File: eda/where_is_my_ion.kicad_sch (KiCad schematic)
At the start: 130 parts, among them J1 USB_C_Receptacle_USB2.0_14P, Q1 Q_NPN, Q2 Q_NPN, SW1 SW_SPST, SW2 SW_SPST, U1 ESP32-C3-WROOM-02, U2 AP2112K-3.3, U3 CP2102N-Axx-xQFN28, U4 TLC59116IPWR, U5 TLC59116IPWR, U6 TLC59116IPWR, U7 TLC59116IPWR, U8 TLC59116IPWR

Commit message: final sch
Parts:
- added C14, C16, C18, C20, C22: 0.1uF ceramic, symbol Device:C
- added C15, C17, C19, C21, C23: 10uF, symbol Device:C
- added D69, D84, D85: LED, symbol Device:LED
- added SW3: FORCE_REFRESH, symbol Switch:SW_Push
- added SW4: NEXT_TRAIN, symbol Switch:SW_Push
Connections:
- net +3V3: now also D68.2 (A), D70.2 (A), D72.2 (A), D73.2 (A), D74.2 (A), D75.2 (A), D76.2 (A), D77.2 (A), D78.2 (A), D79.2 (A), D80.2 (A), D81.2 (A), D82.2 (A), D83.2 (A), U5.2 (A0), U6.3 (A1), U7.2 (A0), U7.3 (A1), U8.4 (A2), C14.1, C15.1, C16.1, C17.1, C18.1, C19.1, C20.1, C21.1, C22.1, C23.1, D69.2 (A), D84.2 (A), D85.2 (A)
- net CHIP_PU: now also C11.2, SW2.2 (B)
- net GND: now also U6.2 (A0), U6.4 (A2), U6.5 (A3), C14.2, C15.2, C16.2, C17.2, C18.2, C19.2, C20.2, C21.2, C22.2, C23.2, SW3.2, SW4.2; no longer U5.2 (A0), U7.2 (A0), U7.3 (A1), U8.4 (A2)
- net IO11: now also SW3.1
- net IO12: now also SW4.1
- net LED_IS_FETCHING: now reaches U5.22 (~{OUT14})
- net LED_IS_FETCHING: now also D69.1 (K)
- net LED_MAP_MODE: now reaches U8.22 (~{OUT14})
- net LED_MAP_MODE: now also D84.1 (K)
- net LED_API_FAILURE: now reaches U8.23 (~{OUT15})
- net LED_API_FAILURE: now also D85.1 (K)
- no-connect marks 21 -> 18
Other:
- note added: "CORE ESP MCU"
- note added: "I2C PULL UP RESISTORS"
- note added: "LED DRIVER 1"
- note added: "LED DRIVER 2"
- note added: "LED DRIVER 3"
- note added: "LED DRIVER 4"
- note added: "LED DRIVER 5"
- note removed: "CORE MODULE"
- moved on the sheet: C1, C10, C11, C2, C3, C4, C5, C6, C7, C8, C9, D1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

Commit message: stuff
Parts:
- removed J1: USB_C_Receptacle_USB2.0_14P, symbol Connector:USB_C_Receptacle_USB2.0_14P
- removed Q1, Q2: Q_NPN, symbol Device:Q_NPN
- added H1, H2, H3, H4: MountingHole, MountingHole:MountingHole_2.2mm_M2, symbol Mechanical:MountingHole
- added J1: USB_C_Receptacle_USB2.0_16P, Connector_USB:USB_C_Receptacle_HRO_TYPE-C-31-M-12, symbol Connector:USB_C_Receptacle_USB2.0_16P
- added Q1, Q2: L8050QLT1G, Package_TO_SOT_SMD:SOT-23, symbol Transistor_BJT:Q_NPN_BEC
- added TP1, TP2, TP3, TP4, TP5, TP6, TP7, TP8, TP9: TestPoint, TestPoint:TestPoint_Pad_D2.0mm, symbol Connector:TestPoint
- C1: renamed from C8; footprint (none) -> Capacitor_Tantalum_SMD:CP_EIA-3528-15_AVX-H; LCSC Part Num. (none) -> C22387953
- C10: renamed from C21; footprint (none) -> Capacitor_Tantalum_SMD:CP_EIA-3528-15_AVX-H
- C11: renamed from C10; footprint (none) -> Capacitor_SMD:C_0805_2012Metric; LCSC Part Num. (none) -> C376929
- C12: renamed from C1; value 10uF -> 10uF/25V; footprint (none) -> Capacitor_Tantalum_SMD:CP_EIA-3528-15_AVX-H; LCSC Part Num. (none) -> C22387953
- C13: renamed from C2; value C -> 0.1uF/50V; footprint (none) -> Capacitor_SMD:C_0603_1608Metric; LCSC Part Num. (none) -> C3011652
- C14: renamed from C3; value C -> 1uF/16V; footprint (none) -> Capacitor_SMD:C_0805_2012Metric; LCSC Part Num. (none) -> C24123
- C15: renamed from C11; footprint (none) -> Capacitor_SMD:C_0805_2012Metric; LCSC Part Num. (none) -> C376929
- C16: renamed from C22; footprint (none) -> Capacitor_SMD:C_0603_1608Metric
- C17: renamed from C23; footprint (none) -> Capacitor_Tantalum_SMD:CP_EIA-3528-15_AVX-H
- C18: renamed from C7; value 10 uFF/25V -> 10 uF/25V; footprint (none) -> Capacitor_Tantalum_SMD:CP_EIA-3528-15_AVX-H
- C19: renamed from C6; footprint (none) -> Capacitor_SMD:C_0603_1608Metric
- C2: renamed from C14; footprint (none) -> Capacitor_SMD:C_0603_1608Metric
- C20: renamed from C4; footprint (none) -> Capacitor_SMD:C_0603_1608Metric
- C21: renamed from C5; footprint (none) -> Capacitor_Tantalum_SMD:CP_EIA-3528-15_AVX-H
- C3: renamed from C15; footprint (none) -> Capacitor_Tantalum_SMD:CP_EIA-3528-15_AVX-H
- C4: renamed from C18; footprint (none) -> Capacitor_SMD:C_0603_1608Metric
- C5: renamed from C19; footprint (none) -> Capacitor_Tantalum_SMD:CP_EIA-3528-15_AVX-H
- C6: renamed from C9; footprint (none) -> Capacitor_SMD:C_0805_2012Metric; LCSC Part Num. (none) -> C24123
- C7: renamed from C16; footprint (none) -> Capacitor_SMD:C_0603_1608Metric
- C8: renamed from C17; footprint (none) -> Capacitor_Tantalum_SMD:CP_EIA-3528-15_AVX-H
- C9: renamed from C20; footprint (none) -> Capacitor_SMD:C_0603_1608Metric
- D1: renamed from D17; value LED -> LED_STN_BLUE; footprint (none) -> LED_SMD:LED_0603_1608Metric; LCSC Part Num. (none) -> C497940
- D10: renamed from D38; value LED -> LED_INTER_WHITE; footprint (none) -> LED_SMD:LED_0603_1608Metric
- D11: renamed from D40; value LED -> LED_INTER_WHITE; footprint (none) -> LED_SMD:LED_0603_1608Metric
- D12: renamed from D42; value LED -> LED_INTER_WHITE; footprint (none) -> LED_SMD:LED_0603_1608Metric
- D13: renamed from D44; value LED -> LED_STN_BLUE; footprint (none) -> LED_SMD:LED_0603_1608Metric
- D14: renamed from D46; value LED -> LED_INTER_WHITE; footprint (none) -> LED_SMD:LED_0603_1608Metric
- D15: renamed from D48; value LED -> LED_INTER_WHITE; footprint (none) -> LED_SMD:LED_0603_1608Metric
- D16: renamed from D50; value LED -> LED_INTER_WHITE; footprint (none) -> LED_SMD:LED_0603_1608Metric
- D17: renamed from D18; value LED -> LED_STN_BLUE; footprint (none) -> LED_SMD:LED_0603_1608Metric
- D18: renamed from D19; value LED -> LED_STN_BLUE; footprint (none) -> LED_SMD:LED_0603_1608Metric
- D19: renamed from D20; value LED -> LED_INTER_WHITE; footprint (none) -> LED_SMD:LED_0603_1608Metric
- D2: renamed from D16; value LED -> LED_INTER_WHITE; footprint (none) -> LED_SMD:LED_0603_1608Metric; LCSC Part Num. (none) -> C965808
- D20: renamed from D21; value LED -> LED_STN_BLUE; footprint (none) -> LED_SMD:LED_0603_1608Metric
- D21: renamed from D10; value LED -> LED_INTER_WHITE; footprint (none) -> LED_SMD:LED_0603_1608Metric
- D22: renamed from D11; value LED -> LED_STN_BLUE; footprint (none) -> LED_SMD:LED_0603_1608Metric
- D23: renamed from D12; value LED -> LED_INTER_WHITE; footprint (none) -> LED_SMD:LED_0603_1608Metric
- D24: renamed from D13; value LED -> LED_INTER_WHITE; footprint (none) -> LED_SMD:LED_0603_1608Metric
- D25, D59, D7, D77: value LED -> LED_INTER_WHITE; footprint (none) -> LED_SMD:LED_0603_1608Metric
- D26: renamed from D39; value LED -> LED_INTER_WHITE; footprint (none) -> LED_SMD:LED_0603_1608Metric
- D27: renamed from D41; value LED -> LED_INTER_WHITE; footprint (none) -> LED_SMD:LED_0603_1608Metric
- D28: renamed from D43; value LED -> LED_STN_BLUE; footprint (none) -> LED_SMD:LED_0603_1608Metric
- D29: renamed from D45; value LED -> LED_INTER_WHITE; footprint (none) -> LED_SMD:LED_0603_1608Metric
- D3: renamed from D15; value LED -> LED_INTER_WHITE; footprint (none) -> LED_SMD:LED_0603_1608Metric
- D30: renamed from D47; value LED -> LED_INTER_WHITE; footprint (none) -> LED_SMD:LED_0603_1608Metric
- D31: renamed from D49; value LED -> LED_INTER_WHITE; footprint (none) -> LED_SMD:LED_0603_1608Metric
- D32: renamed from D51; value LED -> LED_STN_BLUE; footprint (none) -> LED_SMD:LED_0603_1608Metric
- D33: renamed from D22; value LED -> LED_STN_BLUE; footprint (none) -> LED_SMD:LED_0603_1608Metric
- D34: renamed from D24; value LED -> LED_STN_BLUE; footprint (none) -> LED_SMD:LED_0603_1608Metric
- D35: renamed from D26; value LED -> LED_STN_BLUE; footprint (none) -> LED_SMD:LED_0603_1608Metric
- D36: renamed from D28; value LED -> LED_STN_BLUE; footprint (none) -> LED_SMD:LED_0603_1608Metric
- D37: renamed from D30; value LED -> LED_INTER_WHITE; footprint (none) -> LED_SMD:LED_0603_1608Metric
- D38: renamed from D32; value LED -> LED_INTER_WHITE; footprint (none) -> LED_SMD:LED_0603_1608Metric
- D39: renamed from D34; value LED -> LED_STN_BLUE; footprint (none) -> LED_SMD:LED_0603_1608Metric
- D4: renamed from D14; value LED -> LED_INTER_WHITE; footprint (none) -> LED_SMD:LED_0603_1608Metric
- D40: renamed from D36; value LED -> LED_INTER_WHITE; footprint (none) -> LED_SMD:LED_0603_1608Metric
- D41: renamed from D52; value LED -> LED_STN_BLUE; footprint (none) -> LED_SMD:LED_0603_1608Metric
- D42: renamed from D54; value LED -> LED_STN_BLUE; footprint (none) -> LED_SMD:LED_0603_1608Metric
- D43: renamed from D56; value LED -> LED_STN_BLUE; footprint (none) -> LED_SMD:LED_0603_1608Metric
- D44: renamed from D58; value LED -> LED_INTER_WHITE; footprint (none) -> LED_SMD:LED_0603_1608Metric
- D45: renamed from D60; value LED -> LED_INTER_WHITE; footprint (none) -> LED_SMD:LED_0603_1608Metric
- D46: renamed from D62; value LED -> LED_STN_BLUE; footprint (none) -> LED_SMD:LED_0603_1608Metric
- D47: renamed from D64; value LED -> LED_INTER_WHITE; footprint (none) -> LED_SMD:LED_0603_1608Metric
- D48: renamed from D66; value LED -> LED_STN_BLUE; footprint (none) -> LED_SMD:LED_0603_1608Metric
- D49: renamed from D69; value LED -> LED_FETCH_GREEN; footprint (none) -> LED_SMD:LED_0603_1608Metric; LCSC Part Num. (none) -> C7429914
- D5: renamed from D9; value LED -> LED_STN_BLUE; footprint (none) -> LED_SMD:LED_0603_1608Metric
- D50: renamed from D27; value LED -> LED_STN_BLUE; footprint (none) -> LED_SMD:LED_0603_1608Metric
- D51: renamed from D29; value LED -> LED_INTER_WHITE; footprint (none) -> LED_SMD:LED_0603_1608Metric
- D52: renamed from D31; value LED -> LED_INTER_WHITE; footprint (none) -> LED_SMD:LED_0603_1608Metric
- D53: renamed from D33; value LED -> LED_STN_BLUE; footprint (none) -> LED_SMD:LED_0603_1608Metric
- D54: renamed from D35; value LED -> LED_INTER_WHITE; footprint (none) -> LED_SMD:LED_0603_1608Metric
- D55: renamed from D37; value LED -> LED_INTER_WHITE; footprint (none) -> LED_SMD:LED_0603_1608Metric
- D56: renamed from D53; value LED -> LED_INTER_WHITE; footprint (none) -> LED_SMD:LED_0603_1608Metric
- D57: renamed from D55; value LED -> LED_STN_BLUE; footprint (none) -> LED_SMD:LED_0603_1608Metric
- D58: renamed from D57; value LED -> LED_STN_BLUE; footprint (none) -> LED_SMD:LED_0603_1608Metric
- D6: renamed from D8; value LED -> LED_INTER_WHITE; footprint (none) -> LED_SMD:LED_0603_1608Metric
- D60: renamed from D61; value LED -> LED_STN_BLUE; footprint (none) -> LED_SMD:LED_0603_1608Metric
- D61: renamed from D63; value LED -> LED_INTER_WHITE; footprint (none) -> LED_SMD:LED_0603_1608Metric
- D62: renamed from D65; value LED -> LED_INTER_WHITE; footprint (none) -> LED_SMD:LED_0603_1608Metric
- D63: renamed from D67; value LED -> LED_STN_BLUE; footprint (none) -> LED_SMD:LED_0603_1608Metric
- D64: renamed from D68; value LED -> LED_INTER_WHITE; footprint (none) -> LED_SMD:LED_0603_1608Metric
- D65: renamed from D70; value LED -> LED_INTER_WHITE; footprint (none) -> LED_SMD:LED_0603_1608Metric
- D66: renamed from D72; value LED -> LED_STN_BLUE; footprint (none) -> LED_SMD:LED_0603_1608Metric
- D67: renamed from D74; value LED -> LED_INTER_WHITE; footprint (none) -> LED_SMD:LED_0603_1608Metric
- D68: renamed from D76; value LED -> LED_INTER_WHITE; footprint (none) -> LED_SMD:LED_0603_1608Metric
- D69: renamed from D78; value LED -> LED_INTER_WHITE; footprint (none) -> LED_SMD:LED_0603_1608Metric
- D70: renamed from D80; value LED -> LED_INTER_WHITE; footprint (none) -> LED_SMD:LED_0603_1608Metric
- D71: renamed from D82; value LED -> LED_STN_BLUE; footprint (none) -> LED_SMD:LED_0603_1608Metric
- D72: renamed from D2; footprint (none) -> Diode_SMD:D_SOD-123; LCSC Part Num. (none) -> C82544
- D73: renamed from D85; value LED -> LED_API_FAIL_RED; footprint (none) -> LED_SMD:LED_0603_1608Metric
- D74: renamed from D84; value LED -> LED_MAP_MODE_GREEN; footprint (none) -> LED_SMD:LED_0603_1608Metric
- D75: renamed from D73; value LED -> LED_GREEN_WIFI; footprint (none) -> LED_SMD:LED_0603_1608Metric
- D76: renamed from D75; value LED -> LED_STN_BLUE; footprint (none) -> LED_SMD:LED_0603_1608Metric
- D78: renamed from D79; value LED -> LED_INTER_WHITE; footprint (none) -> LED_SMD:LED_0603_1608Metric
- D79: renamed from D81; value LED -> LED_INTER_WHITE; footprint (none) -> LED_SMD:LED_0603_1608Metric
- D8: renamed from D6; value LED -> LED_STN_BLUE; footprint (none) -> LED_SMD:LED_0603_1608Metric
- D80: renamed from D83; value LED -> LED_INTER_WHITE; footprint (none) -> LED_SMD:LED_0603_1608Metric
- D81: renamed from D1; value RED LED -> RED POWER LED; footprint (none) -> LED_SMD:LED_0603_1608Metric; LCSC Part Num. (none) -> C965799
- D82: renamed from D3; footprint (none) -> Diode_SMD:D_SOD-523; LCSC Part Num. (none) -> C383211
- D83: renamed from D4; footprint (none) -> Diode_SMD:D_SOD-523
- D84: renamed from D5; footprint (none) -> Diode_SMD:D_SOD-523
- D9: renamed from D23; value LED -> LED_STN_BLUE; footprint (none) -> LED_SMD:LED_0603_1608Metric
- R1: renamed from R8; footprint (none) -> Resistor_SMD:R_0603_1608Metric; LCSC Part Num. (none) -> C22548
- R10: renamed from R22; footprint (none) -> Resistor_SMD:R_0603_1608Metric
- R11: renamed from R4; footprint (none) -> Resistor_SMD:R_0603_1608Metric
- R12: renamed from R24; footprint (none) -> Resistor_SMD:R_0603_1608Metric
- R13: renamed from R14; footprint (none) -> Resistor_SMD:R_0603_1608Metric
- R14: renamed from R2; footprint (none) -> Resistor_SMD:R_0603_1608Metric
- R15: renamed from R1; footprint (none) -> Resistor_SMD:R_0603_1608Metric
- R16: renamed from R15; footprint (none) -> Resistor_SMD:R_0603_1608Metric
- R17: renamed from R16; footprint (none) -> Resistor_SMD:R_0603_1608Metric
- R18: renamed from R25; footprint (none) -> Resistor_SMD:R_0603_1608Metric
- R19: renamed from R21; footprint (none) -> Resistor_SMD:R_0603_1608Metric
- R2: renamed from R6; footprint (none) -> Resistor_SMD:R_0603_1608Metric
- R20: renamed from R18; footprint (none) -> Resistor_SMD:R_0603_1608Metric
- R21: renamed from R5; footprint (none) -> Resistor_SMD:R_0603_1608Metric
- R22: renamed from R19; footprint (none) -> Resistor_SMD:R_0603_1608Metric
- R23: renamed from R20; footprint (none) -> Resistor_SMD:R_0603_1608Metric
- R24: renamed from R12; footprint (none) -> Resistor_SMD:R_0603_1608Metric
- R25: renamed from R13; footprint (none) -> Resistor_SMD:R_0603_1608Metric
- R3: renamed from R7; footprint (none) -> Resistor_SMD:R_0603_1608Metric
- R4: renamed from R10; footprint (none) -> Resistor_SMD:R_0603_1608Metric; LCSC Part Num. (none) -> C137768
- R5: renamed from R11; footprint (none) -> Resistor_SMD:R_0603_1608Metric; LCSC Part Num. (none) -> C2933225
- R6: renamed from R9; footprint (none) -> Resistor_SMD:R_0603_1608Metric
- R7: renamed from R17; footprint (none) -> Resistor_SMD:R_0603_1608Metric
- R8: renamed from R23; footprint (none) -> Resistor_SMD:R_0603_1608Metric
- R9: renamed from R3; footprint (none) -> Resistor_SMD:R_0603_1608Metric
- SW1: value SW_SPST -> SW_MCU_RESET; footprint (none) -> TS-1088-AR02016:SW_TS-1088-AR02016_1
- SW2: renamed from SW3; footprint (none) -> TS-1088-AR02016:SW_TS-1088-AR02016_1
- SW3: renamed from SW4; footprint (none) -> TS-1088-AR02016:SW_TS-1088-AR02016_1
- SW4: renamed from SW2; value SW_SPST -> SW_BOOT_SEL; footprint (none) -> TS-1088-AR02016:SW_TS-1088-AR02016_1
- renumbered U3 to U1, U4 to U2, U6 to U3, U5 to U4, U7 to U5, U1 to U6, U8 to U7, U2 to U8
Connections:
- net DTR is gone; now on net ~{DTR}: R9.1
- net RTS is gone; now on net ~{RTS}: R11.1
- net +3V3: now also TP3.1
- net +5V: now also U8.3 (EN)
- net CHIP_PU: now also Q1.3 (C)
- net GND: now also J1.A1 (GND), J1.A12 (GND), J1.B1 (GND), J1.B12 (GND), J1.S1 (SHIELD), TP1.1
- net IO10: now also TP8.1
- net IO2: now also TP2.1
- net IO3: now also TP4.1
- net IO4_~{RESET}: now also TP9.1
- net IO5_SDA: now also TP5.1
- net IO6_SCL: now also TP7.1
- net IO7: now also TP6.1
- net IO9: now also Q2.2 (E)
- net U0RXD: now also U6.11 (IO20/RXD)
- net U0TXD: now also U6.12 (IO21/TXD)
- net VBUS: now also J1.A4 (VBUS), J1.A9 (VBUS), J1.B4 (VBUS), J1.B9 (VBUS)
- net ~{DTR}: now also Q2.3 (C)
- net ~{RTS}: now also Q1.2 (E)
- net at D83.2 (A2), R19.1, R20.1: now also J1.A7 (D-)
- net at D84.2 (A2), R22.1, R23.1: now also J1.A6 (D+)
- net at R24.1: now also J1.B5 (CC2)
- net at R11.2: now also Q2.1 (B)
- net at R9.2: now also Q1.1 (B)
- net at R25.1: now also J1.A5 (CC1)
- net IO0 renamed IO0_SW
- net IO0_SW: now also SW2.1
- net IO1 renamed IO1_SW
- net IO1_SW: now also SW3.1
- removed net IO11: SW2.1, U6.11 (IO20/RXD)
- removed net IO12: SW3.1, U6.12 (IO21/TXD)
- no-connect marks 18 -> 20
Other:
- moved on the sheet: C12, C13, C14, C15, R14, R15, SW2, SW3, SW4, U6

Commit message: routing is hard
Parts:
- removed C11, C15: 1 uF/50V (NC), Capacitor_SMD:C_0805_2012Metric, symbol Device:C
- renumbered C12 to C11, C13 to C12, C14 to C13, C16 to C14, C17 to C15, C18 to C16, C19 to C17, C20 to C18, C21 to C19
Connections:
- net USB_D-: now reaches D83.2 (A2), J1.A7 (D-), R19.1, R20.1
- net USB_D+: now reaches D84.2 (A2), J1.A6 (D+), R22.1, R23.1

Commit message: commit
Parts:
- D69, D79: value LED_INTER_WHITE -> LED_STN_BLUE
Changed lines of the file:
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@@
 			)
 		)
-		(property "Value" "LED_INTER_WHITE"
+		(property "Value" "LED_STN_BLUE"
 			(at 554.736 356.108 0)
 			(effects
@@
 			)
 		)
-		(property "Value" "LED_INTER_WHITE"
+		(property "Value" "LED_STN_BLUE"
 			(at 547.116 315.468 0)
 			(effects

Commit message: changes
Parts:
- removed D44: LED_INTER_WHITE, LED_SMD:LED_0603_1608Metric, symbol Device:LED
- added D46: LED_INTER_WHITE, LED_SMD:LED_0603_1608Metric, symbol Device:LED
- renumbered D45 to D44, D46 to D45
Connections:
- net INTER_borden_kmrkt_2 is gone; now on net INTER_borden_kmrkt_1: U5.11 (~{OUT4})
- net +3V3: now also D46.2 (A)
- net INTER_borden_kmrkt_1: no longer U5.9 (~{OUT3})
- net INTER_mill_borden_1: now also U5.8 (~{OUT2}); no longer U5.7 (~{OUT1})
- net STN_REV_BORDEN: now also U5.9 (~{OUT3}); no longer U5.8 (~{OUT2})
- new net INTER_mill_borden_2: D46.1 (K), U5.7 (~{OUT1})
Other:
- moved on the sheet: D44, D45, D47, D48

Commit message: almost done; might have to redo driver2
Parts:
- removed TP2, TP4, TP6, TP8: TestPoint, TestPoint:TestPoint_Pad_D2.0mm, symbol Connector:TestPoint
- renumbered TP3 to TP2, TP5 to TP3, TP7 to TP4, TP9 to TP5

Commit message: might change
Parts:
- added TP10, TP6, TP7, TP8, TP9: TestPoint, TestPoint:TestPoint_Pad_D2.0mm, symbol Connector:TestPoint
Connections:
- net IO0_SW: now also TP6.1
- net IO1_SW: now also TP7.1
- net IO9: now also TP10.1
- net U0RXD: now also TP8.1
- net U0TXD: now also TP9.1

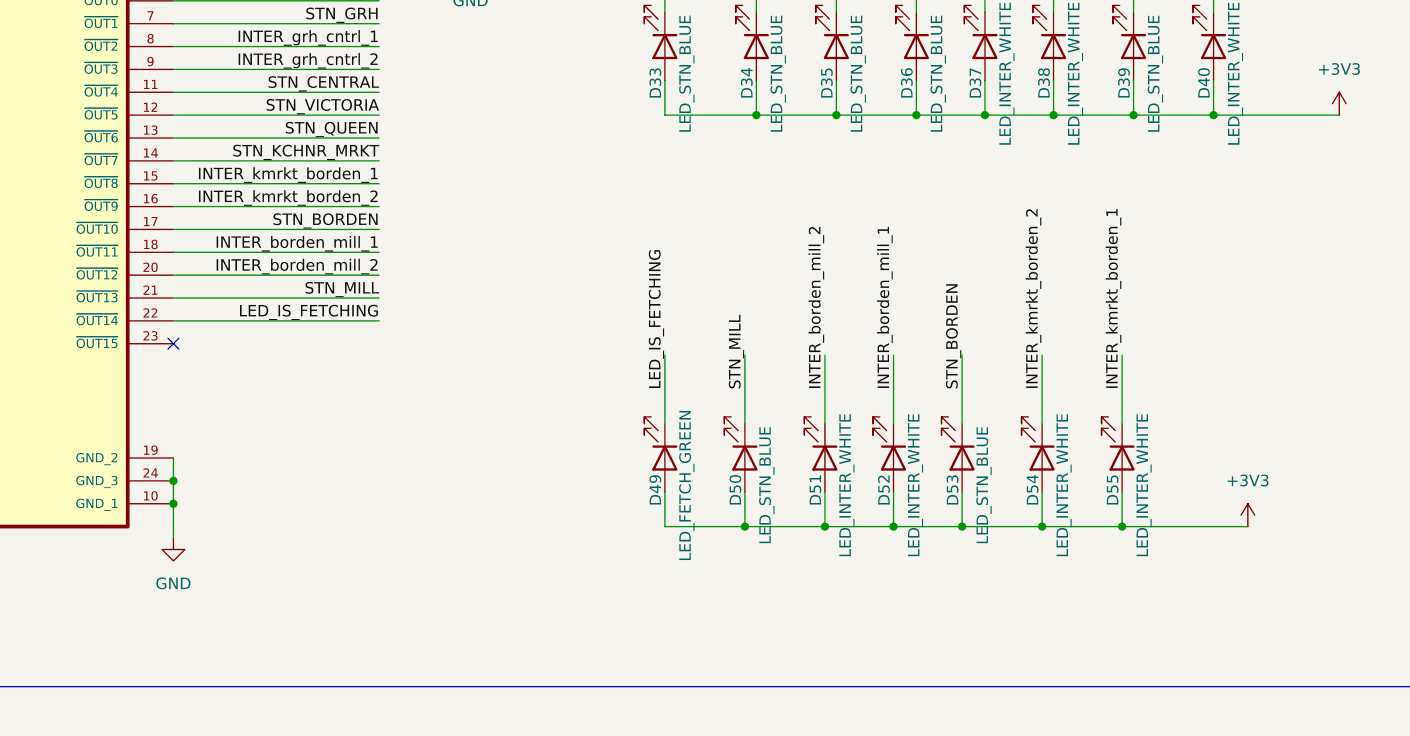
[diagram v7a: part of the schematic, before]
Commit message: side by side layout
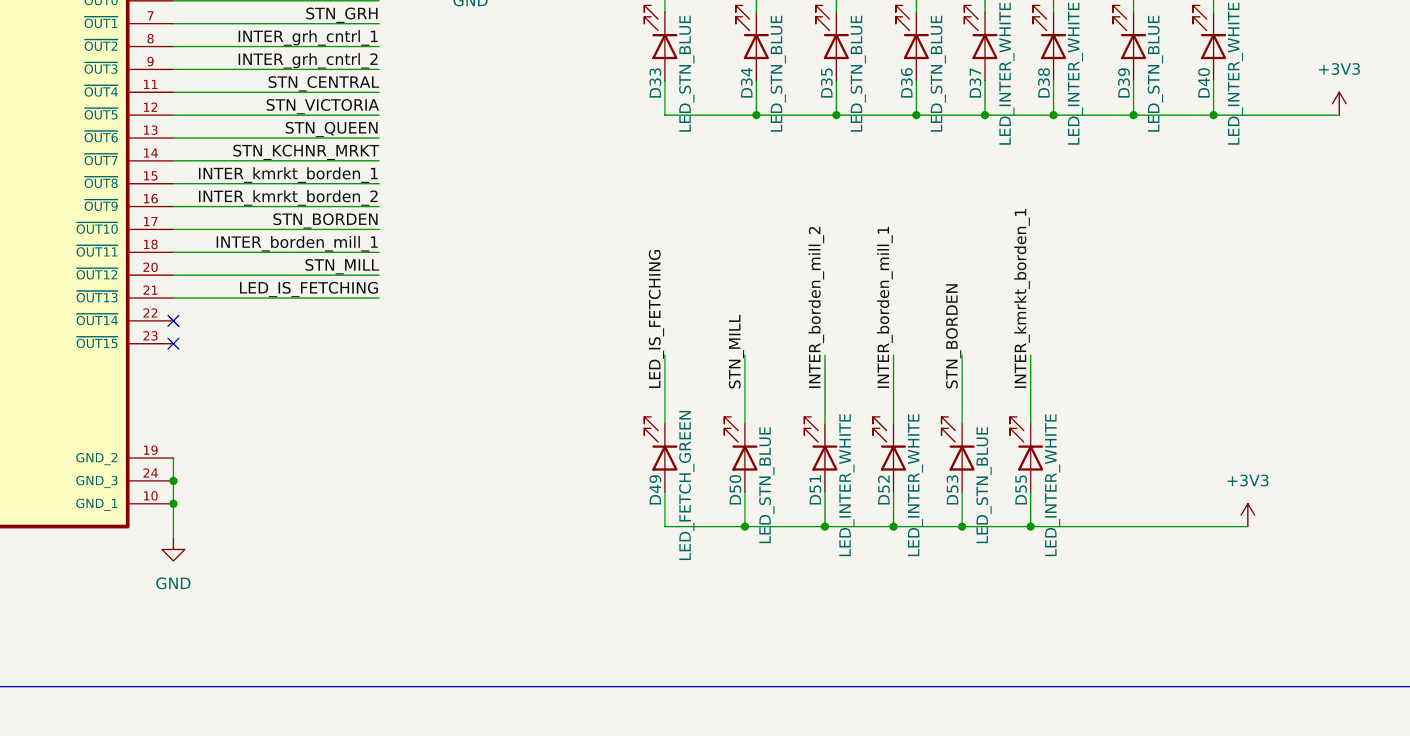
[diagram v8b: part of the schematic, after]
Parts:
- removed D54: LED_INTER_WHITE, LED_SMD:LED_0603_1608Metric, symbol Device:LED
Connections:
- net INTER_borden_mill_2: no longer U4.20 (~{OUT12})
- net LED_IS_FETCHING: now also U4.21 (~{OUT13}); no longer U4.22 (~{OUT14})
- net STN_MILL: now also U4.20 (~{OUT12}); no longer U4.21 (~{OUT13})
- no-connect marks 20 -> 21
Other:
- moved on the sheet: D55
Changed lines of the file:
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@@
 	)
 	(junction
-		(at 332.74 204.47)
+		(at 322.58 204.47)
 		(diameter 0)
 		(color 0 0 0 0)
@@
 	)
 	(junction
-		(at 323.85 204.47)
-		(diameter 0)
-		(color 0 0 0 0)
-	)
-	(junction
 		(at 300.99 102.87)
 		(diameter 0)
@@
 		(at 83.82 44.45)
 	)
+	(no_connect
+		(at 227.33 181.61)
+	)
 	(wire
 		(pts
@@
 	(wire
 		(pts
-			(xy 314.96 204.47) (xy 323.85 204.47)
+			(xy 314.96 204.47) (xy 322.58 204.47)
 		)
 		(stroke
@@
 	(wire
 		(pts
-			(xy 323.85 204.47) (xy 332.74 204.47)
-		)
-		(stroke
-			(width 0)
-			(type default)
-		)
-	)
-	(wire
-		(pts
 			(xy 443.23 66.04) (xy 466.09 66.04)
 		)
@@
 	(wire
 		(pts
-			(xy 323.85 200.66) (xy 323.85 204.47)
-		)
-		(stroke
-			(width 0)
-			(type default)
-		)
-	)
-	(wire
-		(pts
-			(xy 323.85 185.42) (xy 323.85 193.04)
-		)
-		(stroke
-			(width 0)
-			(type default)
-		)
-	)
-	(wire
-		(pts
 			(xy 332.74 52.07) (xy 332.74 55.88)
 		)
@@
 	(wire
 		(pts
-			(xy 227.33 181.61) (xy 250.19 181.61)
-		)
-		(stroke
-			(width 0)
-			(type default)
-		)
-	)
-	(wire
-		(pts
-			(xy 332.74 204.47) (xy 346.71 204.47)
-		)
-		(stroke
-			(width 0)
-			(type default)
-		)
-	)
-	(wire
-		(pts
 			(xy 83.82 59.69) (xy 91.44 59.69)
 		)
@@
 	(wire
 		(pts
-			(xy 332.74 200.66) (xy 332.74 204.47)
+			(xy 322.58 200.66) (xy 322.58 204.47)
 		)
 		(stroke
@@
 	(wire
 		(pts
+			(xy 322.58 204.47) (xy 346.71 204.47)
+		)
+		(stroke
+			(width 0)
+			(type default)
+		)
+	)
+	(wire
+		(pts
 			(xy 562.61 320.04) (xy 576.58 320.04)
 		)
@@
 	(wire
 		(pts
-			(xy 332.74 185.42) (xy 332.74 193.04)
+			(xy 322.58 185.42) (xy 322.58 193.04)
 		)
 		(stroke
@@
 	)
 	(label "INTER_kmrkt_borden_1"
-		(at 332.74 189.23 90)
+		(at 322.58 189.23 90)
 		(effects
 			(font
@@
 	)
 	(label "LED_IS_FETCHING"
-		(at 250.19 181.61 180)
+		(at 250.19 179.07 180)
 		(effects
 			(font
@@
 		)
 	)
-	(label "INTER_kmrkt_borden_2"
-		(at 323.85 189.23 90)
-		(effects
-			(font
-				(size 1.27 1.27)
-			)
-			(justify left bottom)
-		)
-	)
 	(label "INTER_lwp_willis"
 		(at 300.99 87.63 90)
@@
 	)
 	(label "STN_MILL"
-		(at 250.19 179.07 180)
+		(at 250.19 176.53 180)
 		(effects
 			(font
@@
 		)
 	)
-	(label "INTER_borden_mill_2"
-		(at 250.19 176.53 180)
-		(effects
-			(font
-				(size 1.27 1.27)
-			)
-			(justify right bottom)
-		)
-	)
 	(label "IO5_SDA"
 		(at 400.05 91.44 0)
@@
 	(symbol
 		(lib_id "Device:LED")
-		(at 323.85 196.85 270)
-		(unit 1)
-		(exclude_from_sim no)
-		(in_bom yes)
-		(on_board yes)
-		(dnp no)
-		(property "Reference" "D54"
-			(at 322.834 200.406 0)
-			(effects
-				(font
-					(size 1.27 1.27)
-				)
-			)
-		)
-		(property "Value" "LED_INTER_WHITE"
-			(at 326.136 199.898 0)
-			(effects
-				(font
-					(size 1.27 1.27)
-				)
-			)
-		)
-		(property "Footprint" "LED_SMD:LED_0603_1608Metric"
-			(at 323.85 196.85 0)
-			(effects
-				(font
-					(size 1.27 1.27)
-				)
-				(hide yes)
-			)
-		)
-		(property "Datasheet" "~"
-			(at 323.85 196.85 0)
-			(effects
-				(font
-					(size 1.27 1.27)
-				)
-				(hide yes)
-			)
-		)
-		(property "Description" "Light emitting diode"
-			(at 323.85 196.85 0)
-			(effects
-				(font
-					(size 1.27 1.27)
-				)
-				(hide yes)
-			)
-		)
-		(property "Sim.Pins" "1=K 2=A"
-			(at 323.85 196.85 0)
-			(effects
-				(font
-					(size 1.27 1.27)
-				)
-				(hide yes)
-			)
-		)
-		(pin "1"
-		)
-		(pin "2"
-		)
-		(instances
-			(project "where_is_my_ion"
-				(path "/1b7d39dc-ea72-40bd-b392-fed3f2ced69f"
-					(reference "D54")
-					(unit 1)
-				)
-			)
-		)
-	)
-	(symbol
-		(lib_id "Device:LED")
 		(at 553.72 222.25 270)
 		(unit 1)
@@
 	(symbol
 		(lib_id "Device:LED")
-		(at 332.74 196.85 270)
+		(at 322.58 196.85 270)
 		(unit 1)
 		(exclude_from_sim no)
@@
 		(dnp no)
 		(property "Reference" "D55"
-			(at 331.724 200.406 0)
+			(at 321.564 200.406 0)
 			(effects
 				(font
@@
 		)
 		(property "Value" "LED_INTER_WHITE"
-			(at 335.026 199.898 0)
+			(at 324.866 199.898 0)
 			(effects
 				(font
@@
 		)
 		(property "Footprint" "LED_SMD:LED_0603_1608Metric"
-			(at 332.74 196.85 0)
+			(at 322.58 196.85 0)
 			(effects
 				(font
@@
 		)
 		(property "Datasheet" "~"
-			(at 332.74 196.85 0)
+			(at 322.58 196.85 0)
 			(effects
 				(font
@@
 		)
 		(property "Description" "Light emitting diode"
-			(at 332.74 196.85 0)
+			(at 322.58 196.85 0)
 			(effects
 				(font
@@
 		)
 		(property "Sim.Pins" "1=K 2=A"
-			(at 332.74 196.85 0)
+			(at 322.58 196.85 0)
 			(effects
 				(font
